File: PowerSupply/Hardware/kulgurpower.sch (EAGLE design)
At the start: 97 parts, among them X2 1727036

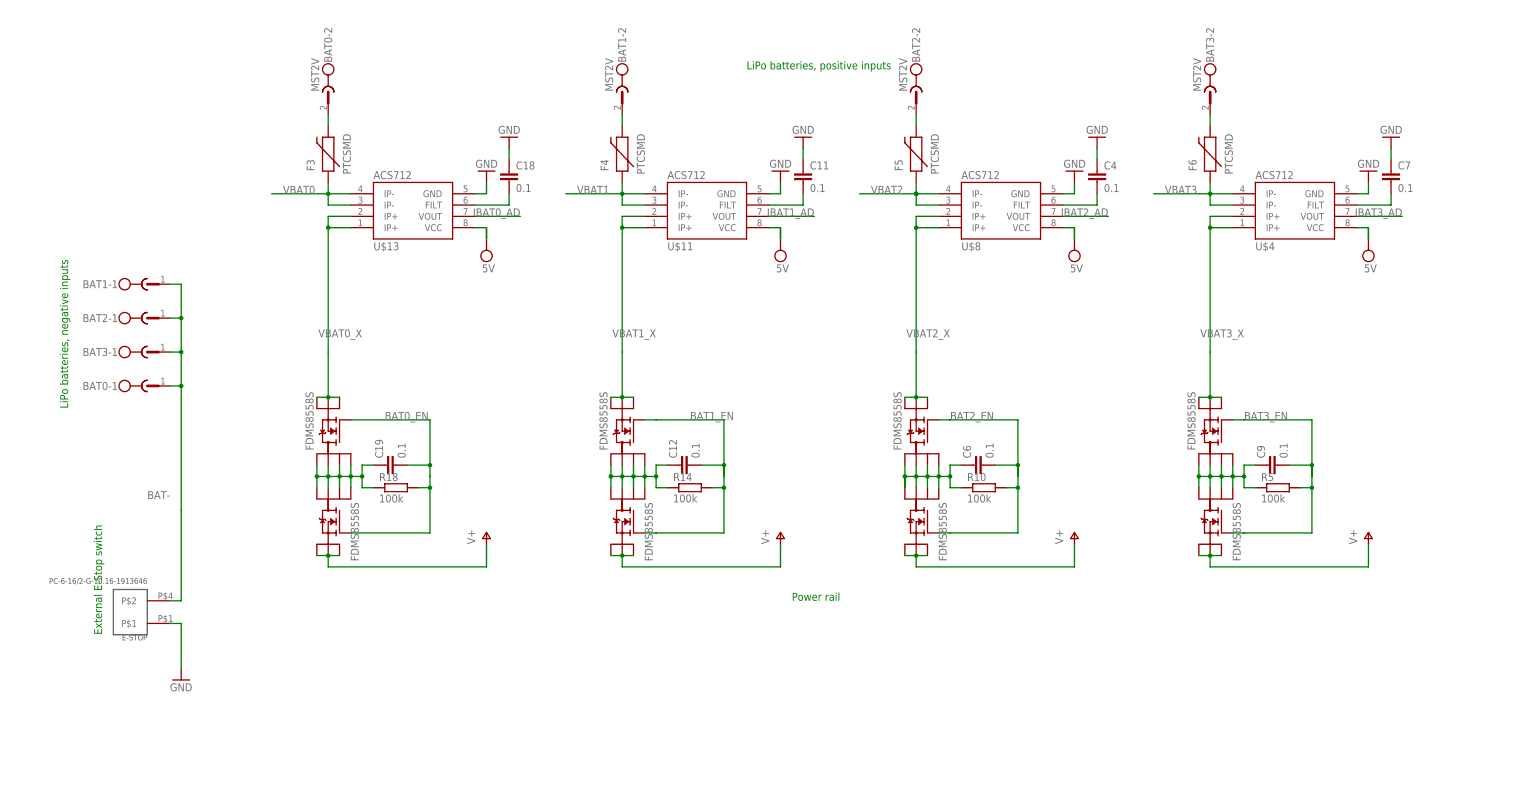
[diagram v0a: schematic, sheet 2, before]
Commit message: More schematics in
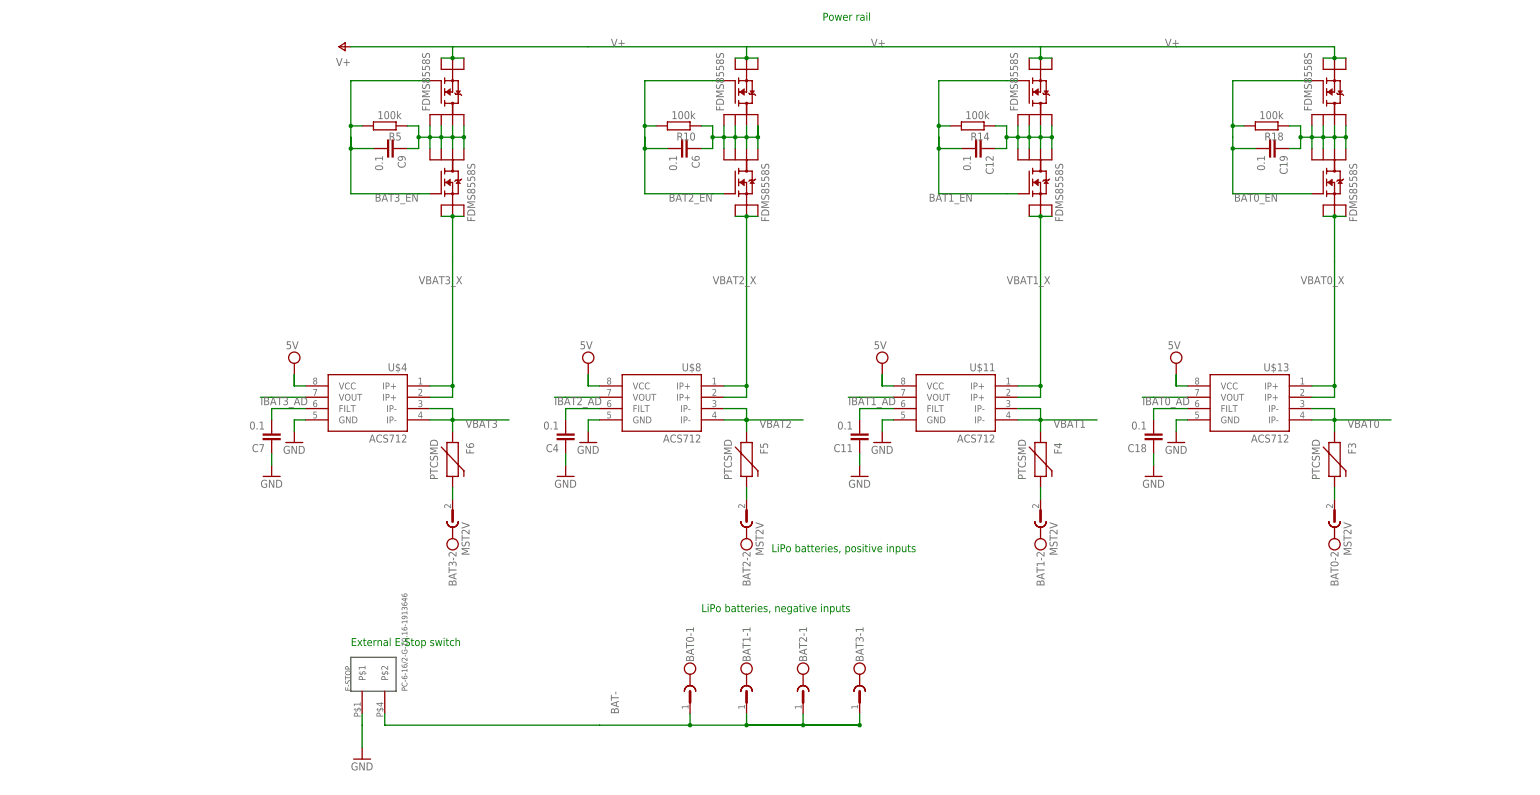
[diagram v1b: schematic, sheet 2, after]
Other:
- note added: "19V In"
- note added: "Battery 0"
- note added: "Battery 1"
- note added: "Battery 2"
- note added: "Battery 3"
- note added: "Output 1"
- note added: "Output 3"
- note added: "Output2"
- moved on the sheet: BAT0-1, BAT0-2, BAT1-1, BAT1-2, BAT2-1, BAT2-2, BAT3-1, BAT3-2, C11, C12, C18, C19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

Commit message: Lot of changes to schematics. A lot.
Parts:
- removed E-STOP: PC-6-16/2-G-10.16-1913646, phoenix-1016:PC-6-16/2-G-10.16-1913646
- removed PWR1, PWR2, PWR3, PWR4, PWR5, PWR6: MST2V, con-phoenix-508:MST2V
- removed R10, R14, R3, R5: 100k, rcl:R-EU_R0603
- removed R4: 680k, rcl:R-EU_R0603
- removed SV2: (no value), con-lstb:MA20-2
- removed TP13: TPB2,54, testpad:TPB2,54
- added C22, C23, C24, C25, C26, C27, C28: 0.1, rcl:C-EUC0603
- added D1, D3: BAT54C, diode:BAT54C
- added M1, M2, M3, M4, MISC, PC: MST2V, con-phoenix-508:MST2V
- added R11, R15, R17, R19: 680k, rcl:R-EU_R0603
- added R13, R16, R20: 100k, rcl:R-EU_R0603
- added SV1: (no value), con-lstb:MA17-2
- added U$20, U$21, U$22, U$23, U$24, U$25, U$26: MAX1614EUA, MAX1614EUA:MAX1614EUA
- added U$27: PC-6-16/2-G-10.16-1913646, phoenix-1016:PC-6-16/2-G-10.16-1913646
- C12, C19, C6, C9: device resistor:C-EUC0603 -> rcl:C-EUC0603
- C2: value 0.1 -> 47uF / 10V; device rcl:C-EUC0603 -> rcl:CPOL-EUC/6032-28R
- F1, F10, F2, F3, F4, F5, F6, F7, F8, F9: value PTCSMD -> 10A FUSE 1206
- U$1, U$10, U$12, U$14, U$15, U$2, U$3, U$5, U$6, U$7, U$9: value FDMS8558S -> AON6500
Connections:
- removed net EN_OUT1: SV2.16, U$1.G
- removed net EN_OUT2: SV2.26, U$14.G
- removed net EN_OUT3: SV2.36, U$15.G
- removed net N$18 (its old number): L2.1, TP5.TP, U$17.VSW
- removed net N$2 (its old number): L1.1, TP8.TP, U$16.VSW
- removed net N$23 (its old number): L3.1, TP10.TP, U$18.VSW
- removed net N$26: L4.1, TP15.TP, U$19.VSW
- removed net PBUS1: F10.1, F7.1, F8.1, F9.1, U$1.S1, U$1.S2, U$1.S3
- removed net PBUS2: F1.1, U$14.S1, U$14.S2, U$14.S3
- removed net PBUS3: F2.1, U$15.S1, U$15.S2, U$15.S3
- removed net SKIP0: SV2.8
- removed net SKIP1: SV2.18
- removed net SKIP2: SV2.28
- removed net SKIP3: SV2.38
- removed net V18V_AD: C2.1, R3.2, R4.2, SV2.6, TP13.TP
- removed net VBB0: C19.1, R18.1, SV2.2, U$12.D1, U$12.D2, U$12.D3, U$12.D4, U$5.D1, U$5.D2, U$5.D3, U$5.D4
- removed net VBB1: C12.1, R14.1, SV2.12, U$10.D1, U$10.D2, U$10.D3, U$10.D4, U$9.D1, U$9.D2, U$9.D3, U$9.D4
- removed net VBB2: C6.1, R10.1, SV2.22, U$6.D1, U$6.D2, U$6.D3, U$6.D4, U$7.D1, U$7.D2, U$7.D3, U$7.D4
- removed net VBB3: C9.1, R5.1, SV2.32, U$2.D1, U$2.D2, U$2.D3, U$2.D4, U$3.D1, U$3.D2, U$3.D3, U$3.D4
- new net !OFF_0: U$20.!LBO, U$20.!OFF
- new net !OFF_1: U$22.!LBO, U$22.!OFF
- new net !OFF_2: U$21.!LBO, U$21.!OFF
- new net !OFF_3: U$23.!LBO, U$23.!OFF
- new net BAT0_G: C19.2, U$12.G, U$20.GATE, U$5.G
- new net BAT0_S: C19.1, U$12.S1, U$12.S2, U$12.S3, U$20.SRC, U$5.S1, U$5.S2, U$5.S3
- new net BAT1_G: C12.2, U$10.G, U$22.GATE, U$9.G
- new net BAT1_S: C12.1, U$10.S1, U$10.S2, U$10.S3, U$22.SRC, U$9.S1, U$9.S2, U$9.S3
- new net BAT2_G: C6.2, U$21.GATE, U$6.G, U$7.G
- new net BAT2_S: C6.1, U$21.SRC, U$6.S1, U$6.S2, U$6.S3, U$7.S1, U$7.S2, U$7.S3
- new net BAT3_G: C9.2, U$2.G, U$23.GATE, U$3.G
- new net BAT3_S: C9.1, U$2.S1, U$2.S2, U$2.S3, U$23.SRC, U$3.S1, U$3.S2, U$3.S3
- new net LBI0: R11.1, R13.2, U$20.LBI
- new net LBI1: R15.1, R16.2, U$22.LBI
- new net LBI2: R17.1, R18.2, U$21.LBI
- new net LBI3: R19.1, R20.2, U$23.LBI
- new net OUT1_EN: SV1.20, U$24.!ON
- new net OUT1_G: C24.2, U$1.G, U$24.GATE
- new net OUT1_S: C24.1, F10.1, F7.1, F8.1, F9.1, U$1.S1, U$1.S2, U$1.S3, U$24.SRC
- new net OUT2_EN: SV1.22, U$25.!ON
- new net OUT2_G: C22.2, U$14.G, U$25.GATE
- new net OUT2_S: C22.1, F1.1, U$14.S1, U$14.S2, U$14.S3, U$25.SRC
- new net OUT3_EN: SV1.24, U$26.!ON
- new net OUT3_G: C23.2, U$15.G, U$26.GATE
- new net OUT3_S: C23.1, F2.1, U$15.S1, U$15.S2, U$15.S3, U$26.SRC
- new net VSW0: L1.1, TP8.TP, U$16.VSW, U$16.VSW1, U$16.VSW2, U$16.VSW3, U$16.VSW4, U$16.VSW5
- new net VSW1: L2.1, TP5.TP, U$17.VSW, U$17.VSW1, U$17.VSW2, U$17.VSW3, U$17.VSW4, U$17.VSW5
- new net VSW2: L3.1, TP10.TP, U$18.VSW, U$18.VSW1, U$18.VSW2, U$18.VSW3, U$18.VSW4, U$18.VSW5
- new net VSW3: L4.1, TP15.TP, U$19.VSW, U$19.VSW1, U$19.VSW2, U$19.VSW3, U$19.VSW4, U$19.VSW5
- net !SKIP0: now also SV1.2
- net !SKIP1: now also SV1.6
- net !SKIP2: now also SV1.10
- net !SKIP3: now also SV1.14
- net +19V: now also D1.CC, D3.CC, SV1.34, U$16.VIN1, U$16.VIN2, U$16.VIN3, U$16.VIN4, U$16.VIN5, U$17.VIN1, U$17.VIN2, U$17.VIN3, U$17.VIN4, U$17.VIN5, U$18.VIN1, U$18.VIN2, U$18.VIN3, U$18.VIN4, U$18.VIN5, U$19.VIN1, U$19.VIN2, U$19.VIN3, U$19.VIN4, U$19.VIN5; no longer R4.1
- net 5V: now also C2.+, C25.2, C26.2, C27.2, C28.2, SV1.17; no longer SV2.15, SV2.25, SV2.35, SV2.5
- net BAT-: now also U$27.B@1, U$27.B@2, U$27.B@3; no longer E-STOP.P$2
- net BAT0_EN: now also D1.A1, SV1.19, U$20.!ON; no longer C19.2, R18.2, SV2.1, U$12.G, U$5.G
- net BAT1_EN: now also D1.A2, SV1.23, U$22.!ON; no longer C12.2, R14.2, SV2.11, U$10.G, U$9.G
- net BAT2_EN: now also D3.A1, SV1.27, U$21.!ON; no longer C6.2, R10.2, SV2.21, U$6.G, U$7.G
- net BAT3_EN: now also D3.A2, SV1.31, U$23.!ON; no longer C9.2, R5.2, SV2.31, U$2.G, U$3.G
- net GND: now also C2.-, C25.1, C26.1, C27.1, C28.1, M1-2.1, M2-2.1, M3-2.1, M4-2.1, MISC-2.1, PC-2.1, R13.1, R16.1, R18.1, R20.1, SV1.11, SV1.12, SV1.15, SV1.16, SV1.3, SV1.4, SV1.7, SV1.8, U$20.GND, U$21.GND, U$22.GND, U$23.GND, U$24.!OFF, U$24.GND, U$24.LBI, U$25.!OFF, U$25.GND, U$25.LBI, U$26.!OFF, U$26.GND, U$26.LBI, U$27.A@1, U$27.A@2, U$27.A@3; no longer C2.2, E-STOP.P$1, PWR1-2.1, PWR2-2.1, PWR3-2.1, PWR4-2.1, PWR5-2.1, PWR6-2.1, R3.1, SV2.10, SV2.19, SV2.20, SV2.29, SV2.30, SV2.39, SV2.40, SV2.9
- net IBAT0_AD: now also SV1.1; no longer SV2.7
- net IBAT1_AD: now also SV1.5; no longer SV2.17
- net IBAT2_AD: now also SV1.9; no longer SV2.27
- net IBAT3_AD: now also SV1.13; no longer SV2.37
- net PWM0: now also SV1.26; no longer SV2.4
- net PWM1: now also SV1.28; no longer SV2.14
- net PWM2: now also SV1.30; no longer SV2.24
- net PWM3: now also SV1.32; no longer SV2.34
- net PWR1: now also M1-1.1; no longer PWR1-1.1
- net PWR2: now also M2-1.1; no longer PWR2-1.1
- net PWR3: now also M3-1.1; no longer PWR3-1.1
- net PWR4: now also M4-1.1; no longer PWR4-1.1
- net PWR5: now also PC-1.1; no longer PWR5-1.1
- net PWR6: now also MISC-1.1; no longer PWR6-1.1
- net V+: now also U$2.D1, U$2.D2, U$2.D3, U$2.D4, U$24.BATT, U$25.BATT, U$26.BATT, U$5.D1, U$5.D2, U$5.D3, U$5.D4, U$6.D1, U$6.D2, U$6.D3, U$6.D4, U$9.D1, U$9.D2, U$9.D3, U$9.D4; no longer U$10.S1, U$10.S2, U$10.S3, U$12.S1, U$12.S2, U$12.S3, U$3.S1, U$3.S2, U$3.S3, U$7.S1, U$7.S2, U$7.S3
- net VBAT0: now also SV1.21; no longer SV2.3
- net VBAT0_X: now also R11.2, U$12.D1, U$12.D2, U$12.D3, U$12.D4, U$20.BATT; no longer U$5.S1, U$5.S2, U$5.S3
- net VBAT1: now also SV1.25; no longer SV2.13
- net VBAT1_X: now also R15.2, U$10.D1, U$10.D2, U$10.D3, U$10.D4, U$22.BATT; no longer U$9.S1, U$9.S2, U$9.S3
- net VBAT2: now also SV1.29; no longer SV2.23
- net VBAT2_X: now also R17.2, U$21.BATT, U$7.D1, U$7.D2, U$7.D3, U$7.D4; no longer U$6.S1, U$6.S2, U$6.S3
- net VBAT3: now also SV1.33; no longer SV2.33
- net VBAT3_X: now also R19.2, U$23.BATT, U$3.D1, U$3.D2, U$3.D3, U$3.D4; no longer U$2.S1, U$2.S2, U$2.S3
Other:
- note added: "5V supply current on this sheet total 40..60mA"
- note added: "5V total max current on this sheet 33mA"
- note added: "680k and 100k make automatic turn off when LiPo is 9.4V"
- note added: "About 100mA of 5V consumption on this board"
- note added: "Hack! !ON! pin of MAX1614 is pulled up by default. Pulling it down enables power. This is achieved using shorting power socket with special tool. Diodes avoid 19V from adapter to flow into !ON! pin which is droven by MCU."
- note added: "LIPO chargers"
- note added: "MOSFET drivers"
- note added: "MOSFET drivers for consumers"
- note added: "MOSFET drivers for four battery inputs"
- note added: "Main input MOSFETs and current sensors"
- note added: "Outputs"
- note added: "Power output to Dynamixels, MCU"
- note added: "Power output to PC"
- note added: "Power outputs to four motors"
- note removed: "19V In"
- note removed: "680 and 100k input divider makes sure 3.3V limit is not exceeded with input voltages up to 25V"
- note removed: "Battery 0"
- note removed: "Battery 1"
- note removed: "Battery 2"
- note removed: "Battery 3"
- note removed: "Just two fuse options on board (1206 and big socket)"
- note removed: "LiPo charger"
- note removed: "Output 1"
- note removed: "Output 3"
- note removed: "Output2"

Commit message: lot of work done on schematics
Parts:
- removed L3, L4: 4,7uH, inductors:DR73
- removed SV1: (no value), con-lstb:MA17-2
- removed TP10, TP15, TP5, TP8: TPB2,54, testpad:TPB2,54
- removed U$16, U$18, U$19: CSD97374Q4M, CSD97374Q4M:CSD97374Q4M
- added C104, C113, C32: 220n, rcl:C-EUC0603
- added C29: 0,1u, rcl:C-EUC0603
- added C30: (no value), rcl:CPOL-EUC/6032-28R
- added C33, C34: 100pF, SparkFun:CAP0805
- added R10, R14, R25, R33: 100k, rcl:R-EU_R0603
- added R21: 120k, rcl:R-EU_R0603
- added R23: 18k, rcl:R-EU_R0603
- added R3: 300k, rcl:R-EU_R0603
- added R31, R32: 3k16, rcl:R-EU_R0603
- added R39, R4, R5: 30k, rcl:R-EU_R0603
- added R40: 270k, rcl:R-EU_R0603
- added SJ100, SJ104, SJ108, SJ110, SJ114: 0R, rcl:R-EU_R0603
- added U$105, U$106, U$107, U$108: IRF8252, tonu:IRF8252
- added X1: 1727036, con-phoenix-3.81:1727036
- added X3, X4: 22-23-2031, con-molex:22-23-2031
- added X5: 22-23-2021, con-molex:22-23-2021
- BAT0, BAT1, BAT2, BAT3, MISC, PC: OC_FARNELL unknown -> (none); OC_NEWARK unknown -> (none)
- C1, C13, C14, C15, C3: value 0.1 -> (none); device rcl:C-EUC0603 -> rcl:CPOL-EUC/6032-28R
- C10: value 0.1 -> 220n
- C16, C20, C21, C8: value 0.1 -> 0,1u
- C17: value 0.1 -> 10uF/6.3V; device rcl:C-EUC0603 -> rcl:C-EUC1210
- C2: value 47uF / 10V -> (none)
- C5: value 0.1 -> 10u; device rcl:C-EUC0603 -> rcl:C-EUC1210
- U$17: value CSD97374Q4M -> TPS51222RTVT; device CSD97374Q4M:CSD97374Q4M -> tps51222:TPS51222RTVT
- X2: value 1727036 -> 2534-; device con-phoenix-3.81:1727036 -> con-3m:2534-
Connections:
- removed net !SKIP0: SV1.2, U$16.!SKIP
- removed net !SKIP1: SV1.6, U$17.!SKIP
- removed net !SKIP2: SV1.10, U$18.!SKIP
- removed net !SKIP3: SV1.14, U$19.!SKIP
- removed net N$2: C8.1, U$17.BOOT
- removed net N$20: C17.2, U$19.BOOT_R
- removed net N$22: C1.2, U$16.BOOT_R
- removed net N$23: C14.1, U$18.BOOT
- removed net N$3: C8.2, U$17.BOOT_R
- removed net PWM0: SV1.26, U$16.PWM
- removed net PWM1: SV1.28, U$17.PWM
- removed net PWM2: SV1.30, U$18.PWM
- removed net PWM3: SV1.32, U$19.PWM
- removed net VSW0: L1.1, TP8.TP, U$16.VSW, U$16.VSW1, U$16.VSW2, U$16.VSW3, U$16.VSW4, U$16.VSW5
- removed net VSW1: L2.1, TP5.TP, U$17.VSW, U$17.VSW1, U$17.VSW2, U$17.VSW3, U$17.VSW4, U$17.VSW5
- removed net VSW2: L3.1, TP10.TP, U$18.VSW, U$18.VSW1, U$18.VSW2, U$18.VSW3, U$18.VSW4, U$18.VSW5
- removed net VSW3: L4.1, TP15.TP, U$19.VSW, U$19.VSW1, U$19.VSW2, U$19.VSW3, U$19.VSW4, U$19.VSW5
- new net +5V: C1.+, C113.1, C13.+, L1.1, SJ114.2, X1-1.1
- new net COMP1: C34.1, R23.1, U$17.COMP1
- new net COMP2: C33.1, R39.2, U$17.COMP2
- new net COMPUTER_PWR: X2-28.KL, X5-2.S
- new net CSN1: C16.1, R21.2, R25.2, SJ114.1, U$17.CSN1, U$17.V5SW
- new net CSN2: C20.1, R33.1, R40.2, SJ100.1, U$17.CSN2
- new net CSP1: C16.2, R25.1, R31.1, U$17.CSP1
- new net CSP2: C20.2, R32.1, R33.2, U$17.CSP2
- new net DRVH1: U$105.G, U$17.DRVH1
- new net DRVH2: U$108.G, U$17.DRVH2
- new net DRVL1: U$106.G, U$17.DRVL1
- new net DRVL2: U$107.G, U$17.DRVL2
- new net ENABLE_PWR: U$17.EN, X2-30.KL
- new net IMON1: U$17.IMON1, X2-27.KL
- new net IMON2: U$17.IMON2, X2-29.KL
- new net N$29: C8.1, U$17.VBST1
- new net N$30: C21.1, U$17.VBST
- new net OUT4_EN: U$17.EN1, X2-24.KL
- new net OUT5_EN: U$17.EN2, X2-26.KL
- new net PGOOD1: R10.2, U$17.PGOOD1, X2-31.KL
- new net PGOOD2: R14.2, U$17.PGOOD2, X2-33.KL
- new net PWM_A: X2-34.KL, X3-3.S
- new net PWM_B: X2-32.KL, X4-3.S
- new net SERVO: C104.1, C14.+, C15.+, C2.+, C30.+, L2.2, SJ100.2, X1-3.1, X3-2.S, X4-2.S
- new net SW1: C8.2, R31.2, SJ108.1, U$17.SW1
- new net SW2: C21.2, R32.2, SJ110.1, U$17.SW2
- new net VIN: SJ104.1, U$17.VIN
- new net VREF2: C10.1, C33.2, C34.2, R23.2, R39.1, U$17.SKIPSEL1, U$17.SKIPSEL2, U$17.VREF2
- new net VREG3: C17.2, R10.1, R14.1, U$17.VREG3
- new net X1: L1.2, SJ108.2, U$105.S@1, U$105.S@2, U$105.S@3, U$106.D@1, U$106.D@2, U$106.D@3, U$106.D@4
- new net X2: L2.1, SJ110.2, U$107.D@1, U$107.D@2, U$107.D@3, U$107.D@4, U$108.S@1, U$108.S@2, U$108.S@3
- net +19V: now also X2-14.KL, X2-16.KL; no longer C13.1, C16.1, C21.1, C5.1, SV1.34, U$16.VIN, U$16.VIN1, U$16.VIN2, U$16.VIN3, U$16.VIN4, U$16.VIN5, U$17.VIN, U$17.VIN1, U$17.VIN2, U$17.VIN3, U$17.VIN4, U$17.VIN5, U$18.VIN, U$18.VIN1, U$18.VIN2, U$18.VIN3, U$18.VIN4, U$18.VIN5, U$19.VIN, U$19.VIN1, U$19.VIN2, U$19.VIN3, U$19.VIN4, U$19.VIN5, X2-1.1
- net 5V: now also C5.2, U$17.VREG5; no longer C10.1, C15.1, C2.+, C20.1, C3.1, SV1.17, U$16.VDD, U$17.VDD, U$18.VDD, U$19.VDD
- net BAT0_EN: now also X2-9.KL; no longer SV1.19
- net BAT1_EN: now also X2-11.KL; no longer SV1.23
- net BAT2_EN: now also X2-13.KL; no longer SV1.27
- net BAT3_EN: now also X2-15.KL; no longer SV1.31
- net GND: now also C1.-, C104.2, C113.2, C13.-, C14.-, C15.-, C17.1, C29.1, C3.-, C30.-, C32.2, C5.1, R3.1, R4.1, R5.1, U$106.S@1, U$106.S@2, U$106.S@3, U$107.S@1, U$107.S@2, U$107.S@3, U$17.TAB, X1-2.1, X1-4.1, X2-10.KL, X2-17.KL, X3-1.S, X4-1.S, X5-1.S; no longer C13.2, C15.2, C16.2, C20.2, C21.2, C3.2, C5.2, SV1.11, SV1.12, SV1.15, SV1.16, SV1.3, SV1.4, SV1.7, SV1.8, U$16.GND, U$16.PAD, U$17.PAD, U$18.GND, U$18.PAD, U$19.GND, U$19.PAD, X2-2.1
- net IBAT0_AD: now also X2-19.KL; no longer SV1.1
- net IBAT1_AD: now also X2-21.KL; no longer SV1.5
- net IBAT2_AD: now also X2-23.KL; no longer SV1.9
- net IBAT3_AD: now also X2-25.KL; no longer SV1.13
- net N$18: now also R40.1, R5.2, U$17.VFB2; no longer C17.1, U$19.BOOT
- net N$24: now also R3.2, U$17.RF; no longer C14.2, U$18.BOOT_R
- net N$5: now also R21.1, R4.2, U$17.VFB1; no longer C1.1, U$16.BOOT
- net OUT1_EN: now also X2-18.KL; no longer SV1.20
- net OUT2_EN: now also X2-20.KL; no longer SV1.22
- net OUT3_EN: now also X2-22.KL; no longer SV1.24
- net V+: now also C29.2, C3.+, C32.1, SJ104.2, U$105.D@1, U$105.D@2, U$105.D@3, U$105.D@4, U$108.D@1, U$108.D@2, U$108.D@3, U$108.D@4, X2-12.KL
- net VBAT0: now also X2-1.KL, X2-2.KL; no longer SV1.21
- net VBAT0_X: no longer L1.2
- net VBAT1: now also X2-3.KL, X2-4.KL; no longer SV1.25
- net VBAT1_X: no longer L2.2
- net VBAT2: now also X2-5.KL, X2-6.KL; no longer SV1.29
- net VBAT2_X: no longer L3.2
- net VBAT3: now also X2-7.KL, X2-8.KL; no longer SV1.33
- net VBAT3_X: no longer L4.2
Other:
- note added: "+5V, +10V power supplies"
- note added: "3,3V 10mA"
- note added: "5v 100mA"
- note added: "R1 = (VOUT -1.0) * R2 120 = 4 * 30"
- note added: "R1 = (VOUT -1.0) * R2 270 = 9 * 30"
- note removed: "19V from wall adapter"
- note removed: "5V total max current on this sheet 33mA"
- note removed: "About 100mA of 5V consumption on this board"
- note removed: "LIPO chargers"

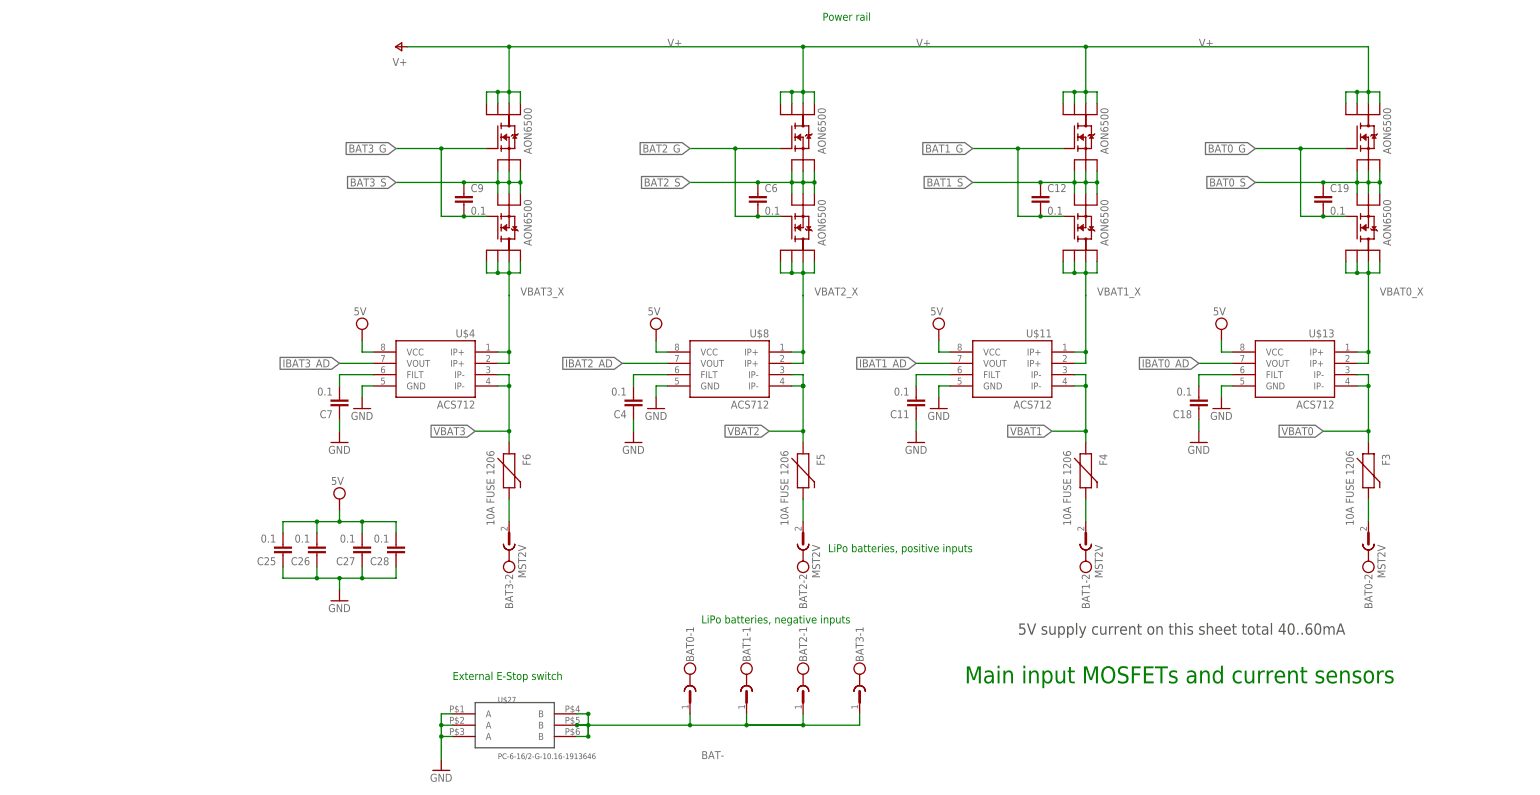
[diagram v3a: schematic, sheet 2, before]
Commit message: Converted into 2 layer board from 4 layer. Seems to be OK for production
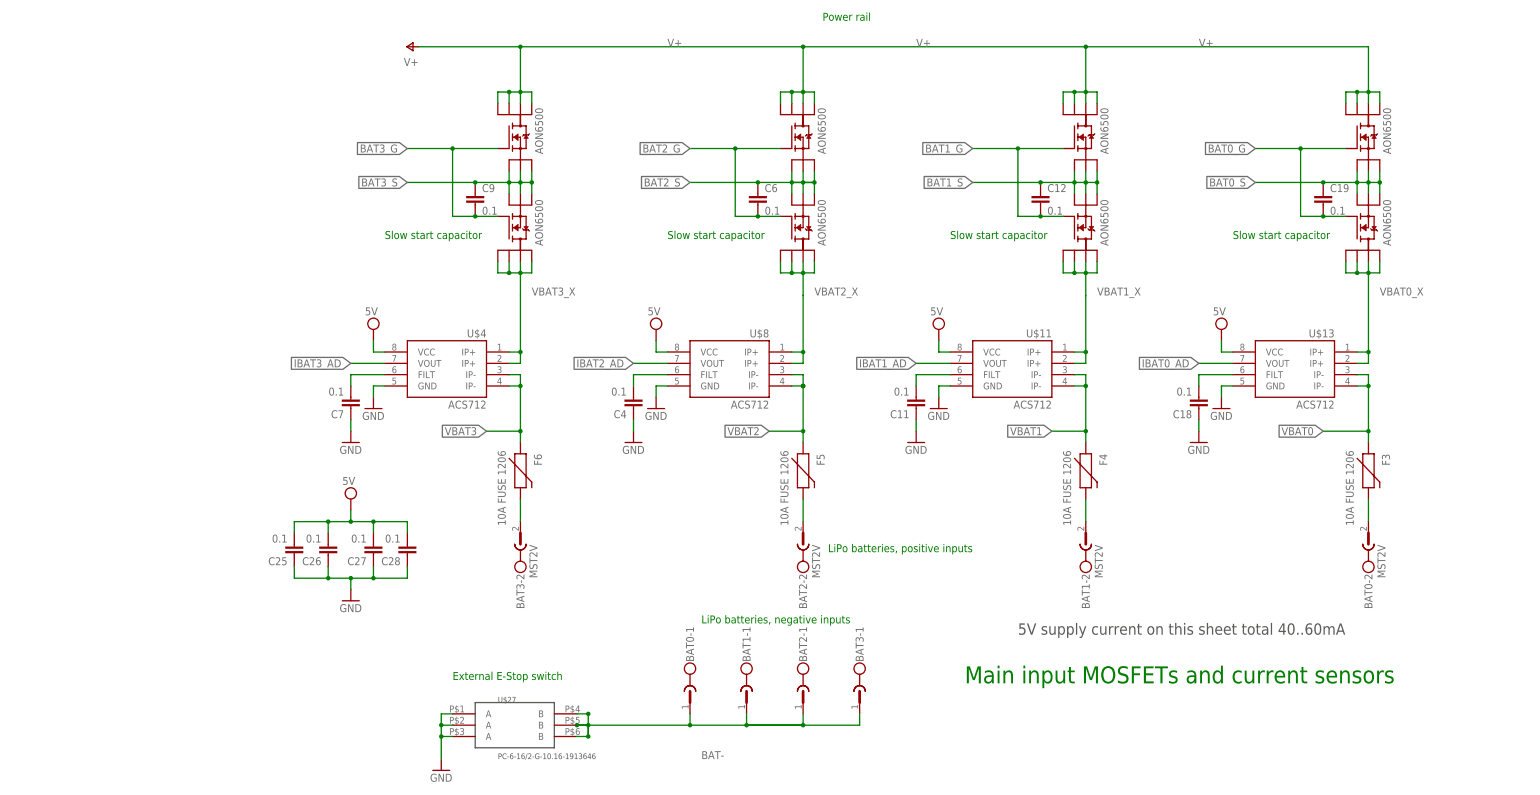
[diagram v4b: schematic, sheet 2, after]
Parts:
- added PC1: MST2V, con-phoenix-508:MST2V
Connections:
- net +19V: now also PC1-2.1
- net GND: now also PC1-1.1
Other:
- note added: "Slow start capacitor"
- moved on the sheet: BAT3-2, C25, C26, C27, C28, C7, C9, F6, U$107, U$108, U$4, X3-1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
